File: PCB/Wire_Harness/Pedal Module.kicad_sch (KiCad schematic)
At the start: 2 parts, among them J13 Motor Controller 12-pin, J14 Motor Controller 20-pin

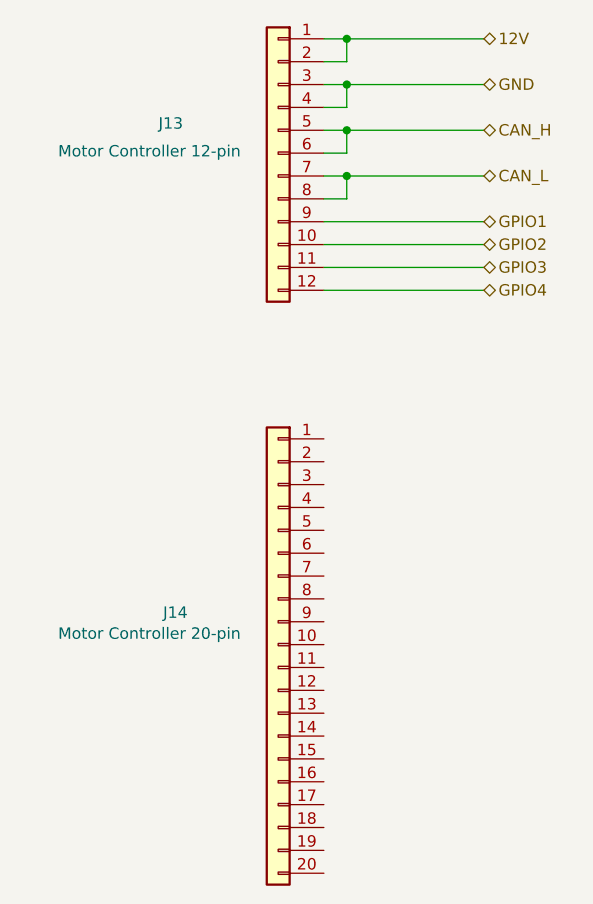
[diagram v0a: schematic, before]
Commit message: changed schematic size to 11x17, added part numbers for enclosures and connectors
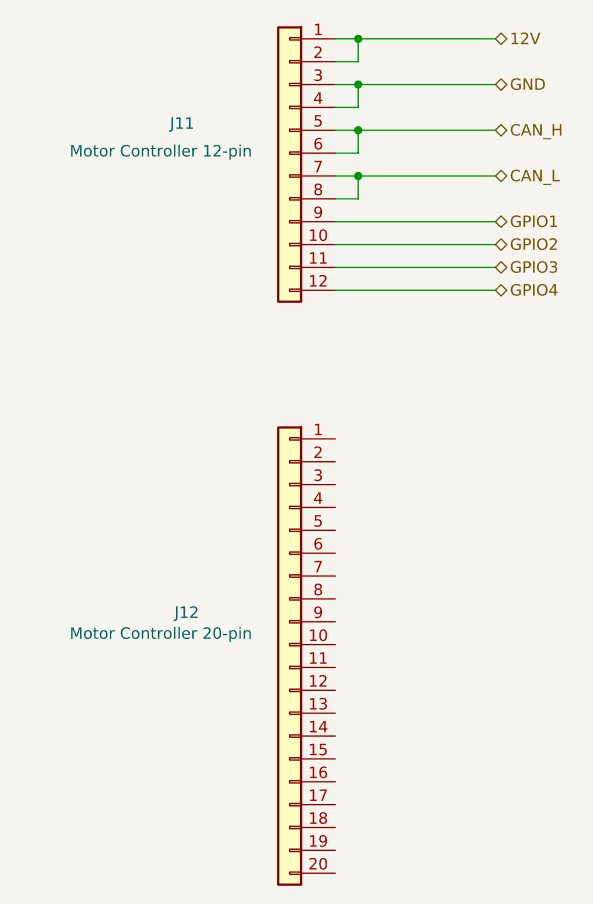
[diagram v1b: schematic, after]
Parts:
- removed J13: Motor Controller 12-pin, symbol VMS_Symbols:Conn_01x12
- removed J14: Motor Controller 20-pin, symbol VMS_Symbols:Conn_01x20
- added J11: Motor Controller 12-pin, symbol VMS_Symbols:Conn_01x12
- added J12: Motor Controller 20-pin, symbol VMS_Symbols:Conn_01x20
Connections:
- net 12V: now also J11.1 (Pin_1), J11.2 (Pin_2)
- net CAN_H: now also J11.5 (Pin_5), J11.6 (Pin_6)
- net CAN_L: now also J11.7 (Pin_7), J11.8 (Pin_8)
- net GND: now also J11.3 (Pin_3), J11.4 (Pin_4)
- net GPIO1: now also J11.9 (Pin_9)
- net GPIO2: now also J11.10 (Pin_10)
- net GPIO3: now also J11.11 (Pin_11)
- net GPIO4: now also J11.12 (Pin_12)
